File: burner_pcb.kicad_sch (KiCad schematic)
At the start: 46 parts, among them J1 Pairing Button, U1 TPS542A50RJMR, U2 SQJB80EP-T1_GE3, U3 MCP6001UT-I/OT, U4 AP62200WU-7, U5 ESP32-WROOM-E, U6 ACS711KEXLT-31AB-T, U7 ACS711KEXLT-31AB-T, U8 MCP6001UT-I/OT

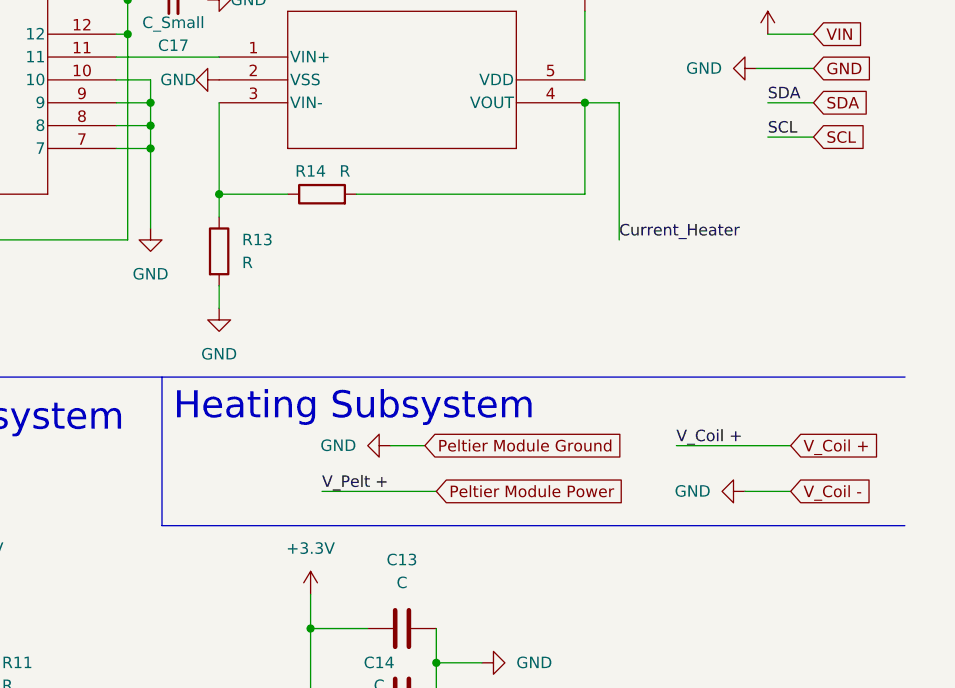
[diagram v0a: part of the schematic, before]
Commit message: added subsystem kicad screenshots
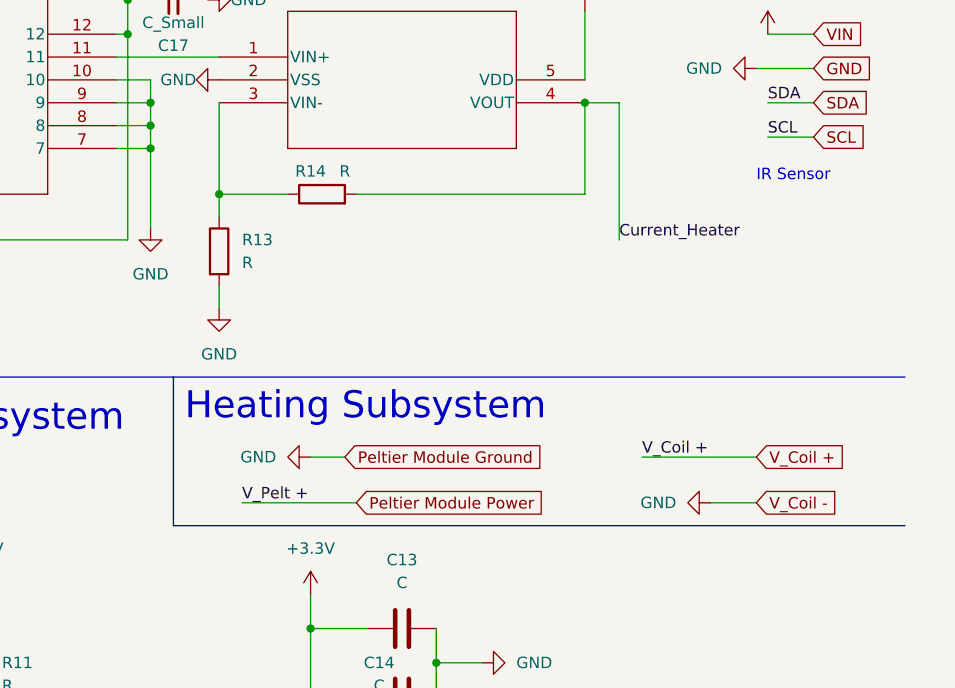
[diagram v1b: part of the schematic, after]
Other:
- note added: "IR Sensor"
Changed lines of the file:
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@@
     (stroke (width 0) (type default))
   )
-  (wire (pts (xy 266.7 82.55) (xy 271.78 82.55))
+  (wire (pts (xy 262.89 83.82) (xy 267.97 83.82))
     (stroke (width 0) (type default))
   )
@@
     (stroke (width 0) (type default))
   )
-  (polyline (pts (xy 201.93 86.36) (xy 284.48 86.36))
+  (polyline (pts (xy 203.2 86.36) (xy 284.48 86.36))
     (stroke (width 0) (type default))
   )
@@
     (stroke (width 0) (type default))
   )
-  (wire (pts (xy 259.08 77.47) (xy 271.78 77.47))
+  (wire (pts (xy 255.27 78.74) (xy 267.97 78.74))
     (stroke (width 0) (type default))
   )
@@
     (stroke (width 0) (type default))
   )
-  (wire (pts (xy 219.71 82.55) (xy 232.41 82.55))
+  (wire (pts (xy 210.82 83.82) (xy 223.52 83.82))
     (stroke (width 0) (type default))
   )
@@
     (stroke (width 0) (type default))
   )
-  (polyline (pts (xy 201.93 69.85) (xy 201.93 86.36))
+  (polyline (pts (xy 203.2 69.85) (xy 203.2 86.36))
     (stroke (width 0) (type default))
   )
@@
     (stroke (width 0) (type default))
   )
-  (wire (pts (xy 227.33 77.47) (xy 231.14 77.47))
+  (wire (pts (xy 218.44 78.74) (xy 222.25 78.74))
     (stroke (width 0) (type default))
   )
@@
     (stroke (width 0) (type default))
   )
-  (text "Heating Subsystem" (at 203.2 74.93 0)
+  (text "Heating Subsystem" (at 204.47 74.93 0)
     (effects (font (size 3 3)) (justify left bottom))
   )
@@
     (effects (font (size 1.27 1.27)) (justify left bottom))
   )
+  (text "IR Sensor" (at 267.97 48.26 0)
+    (effects (font (size 1.27 1.27)) (justify left bottom))
+  )
   (text "12V-3.3V 2A Converter -> Sensor, Control" (at 58.42 76.2 0)
     (effects (font (size 1.27 1.27)) (justify left bottom))
@@
     (effects (font (size 1.27 1.27)) (justify left bottom))
   )
-  (label "V_Coil +" (at 259.08 77.47 0) (fields_autoplaced)
+  (label "V_Coil +" (at 255.27 78.74 0) (fields_autoplaced)
     (effects (font (size 1.27 1.27)) (justify left bottom))
   )
@@
     (effects (font (size 1.27 1.27)) (justify left bottom))
   )
-  (label "V_Pelt +" (at 219.71 82.55 0) (fields_autoplaced)
+  (label "V_Pelt +" (at 210.82 83.82 0) (fields_autoplaced)
     (effects (font (size 1.27 1.27)) (justify left bottom))
   )
@@
     (effects (font (size 1.27 1.27)) (justify left bottom))
   )
-  (global_label "V_Coil +" (shape input) (at 271.78 77.47 0) (fields_autoplaced)
+  (global_label "V_Coil +" (shape input) (at 267.97 78.74 0) (fields_autoplaced)
     (effects (font (size 1.27 1.27)) (justify left))
-    (property "Intersheetrefs" "${INTERSHEET_REFS}" (at 283.0504 77.47 0)
+    (property "Intersheetrefs" "${INTERSHEET_REFS}" (at 279.2404 78.74 0)
       (effects (font (size 1.27 1.27)) (justify left) hide)
     )
@@
     )
   )
-  (global_label "Peltier Module Power" (shape input) (at 232.41 82.55 0) (fields_autoplaced)
+  (global_label "Peltier Module Power" (shape input) (at 223.52 83.82 0) (fields_autoplaced)
     (effects (font (size 1.27 1.27)) (justify left))
-    (property "Intersheetrefs" "${INTERSHEET_REFS}" (at 255.836 82.55 0)
+    (property "Intersheetrefs" "${INTERSHEET_REFS}" (at 246.946 83.82 0)
       (effects (font (size 1.27 1.27)) (justify left) hide)
     )
   )
-  (global_label "Peltier Module Ground" (shape input) (at 231.14 77.47 0) (fields_autoplaced)
+  (global_label "Peltier Module Ground" (shape input) (at 222.25 78.74 0) (fields_autoplaced)
     (effects (font (size 1.27 1.27)) (justify left))
-    (property "Intersheetrefs" "${INTERSHEET_REFS}" (at 255.5939 77.47 0)
+    (property "Intersheetrefs" "${INTERSHEET_REFS}" (at 246.7039 78.74 0)
       (effects (font (size 1.27 1.27)) (justify left) hide)
     )
@@
     )
   )
-  (global_label "V_Coil -" (shape input) (at 271.78 82.55 0) (fields_autoplaced)
+  (global_label "V_Coil -" (shape input) (at 267.97 83.82 0) (fields_autoplaced)
     (effects (font (size 1.27 1.27)) (justify left))
-    (property "Intersheetrefs" "${INTERSHEET_REFS}" (at 283.0504 82.55 0)
+    (property "Intersheetrefs" "${INTERSHEET_REFS}" (at 279.2404 83.82 0)
       (effects (font (size 1.27 1.27)) (justify left) hide)
     )
@@
     )
   )
-  (symbol (lib_id "power:GND") (at 266.7 82.55 270) (unit 1)
+  (symbol (lib_id "power:GND") (at 262.89 83.82 270) (unit 1)
     (in_bom yes) (on_board yes) (dnp no)
-    (property "Reference" "#PWR035" (at 260.35 82.55 0)
-      (effects (font (size 1.27 1.27)) hide)
-    )
-    (property "Value" "GND" (at 262.89 82.55 90)
+    (property "Reference" "#PWR035" (at 256.54 83.82 0)
+      (effects (font (size 1.27 1.27)) hide)
+    )
+    (property "Value" "GND" (at 259.08 83.82 90)
       (effects (font (size 1.27 1.27)) (justify right))
     )
-    (property "Footprint" "" (at 266.7 82.55 0)
-      (effects (font (size 1.27 1.27)) hide)
-    )
-    (property "Datasheet" "" (at 266.7 82.55 0)
+    (property "Footprint" "" (at 262.89 83.82 0)
+      (effects (font (size 1.27 1.27)) hide)
+    )
+    (property "Datasheet" "" (at 262.89 83.82 0)
       (effects (font (size 1.27 1.27)) hide)
     )
@@
     )
   )
-  (symbol (lib_id "power:GND") (at 227.33 77.47 270) (unit 1)
-    (in_bom yes) (on_board yes) (dnp no) (fields_autoplaced)
-    (property "Reference" "#PWR011" (at 220.98 77.47 0)
-      (effects (font (size 1.27 1.27)) hide)
-    )
-    (property "Value" "GND" (at 223.52 77.47 90)
+  (symbol (lib_id "power:GND") (at 218.44 78.74 270) (unit 1)
+    (in_bom yes) (on_board yes) (dnp no) (fields_autoplaced)
+    (property "Reference" "#PWR011" (at 212.09 78.74 0)
+      (effects (font (size 1.27 1.27)) hide)
+    )
+    (property "Value" "GND" (at 214.63 78.74 90)
       (effects (font (size 1.27 1.27)) (justify right))
     )
-    (property "Footprint" "" (at 227.33 77.47 0)
-      (effects (font (size 1.27 1.27)) hide)
-    )
-    (property "Datasheet" "" (at 227.33 77.47 0)
-      (effects (font (size 1.27 1.27)) hide)
-    )
+    (property "Footprint" "" (at 218.44 78.74 0)
+      (effects (font (size 1.27 1.27)) hide)
+    )
+    (property "Datasheet" "" (at 218.44 78.74 0)
+      (effects (font (size 1.27 1.27)) hide)
+    )
